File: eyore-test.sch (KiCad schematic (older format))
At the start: 29 parts, among them P1 USB_5PIN_SHELL, P2 CONN_01X04, P3 CONN_01X02, SW1 SW_PUSHBUTTON, SW2 SW_PUSHBUTTON, U1 LD1117S33CTR, U2 STM32F072C8, U3 ESP-12E, U4 ESP-12E

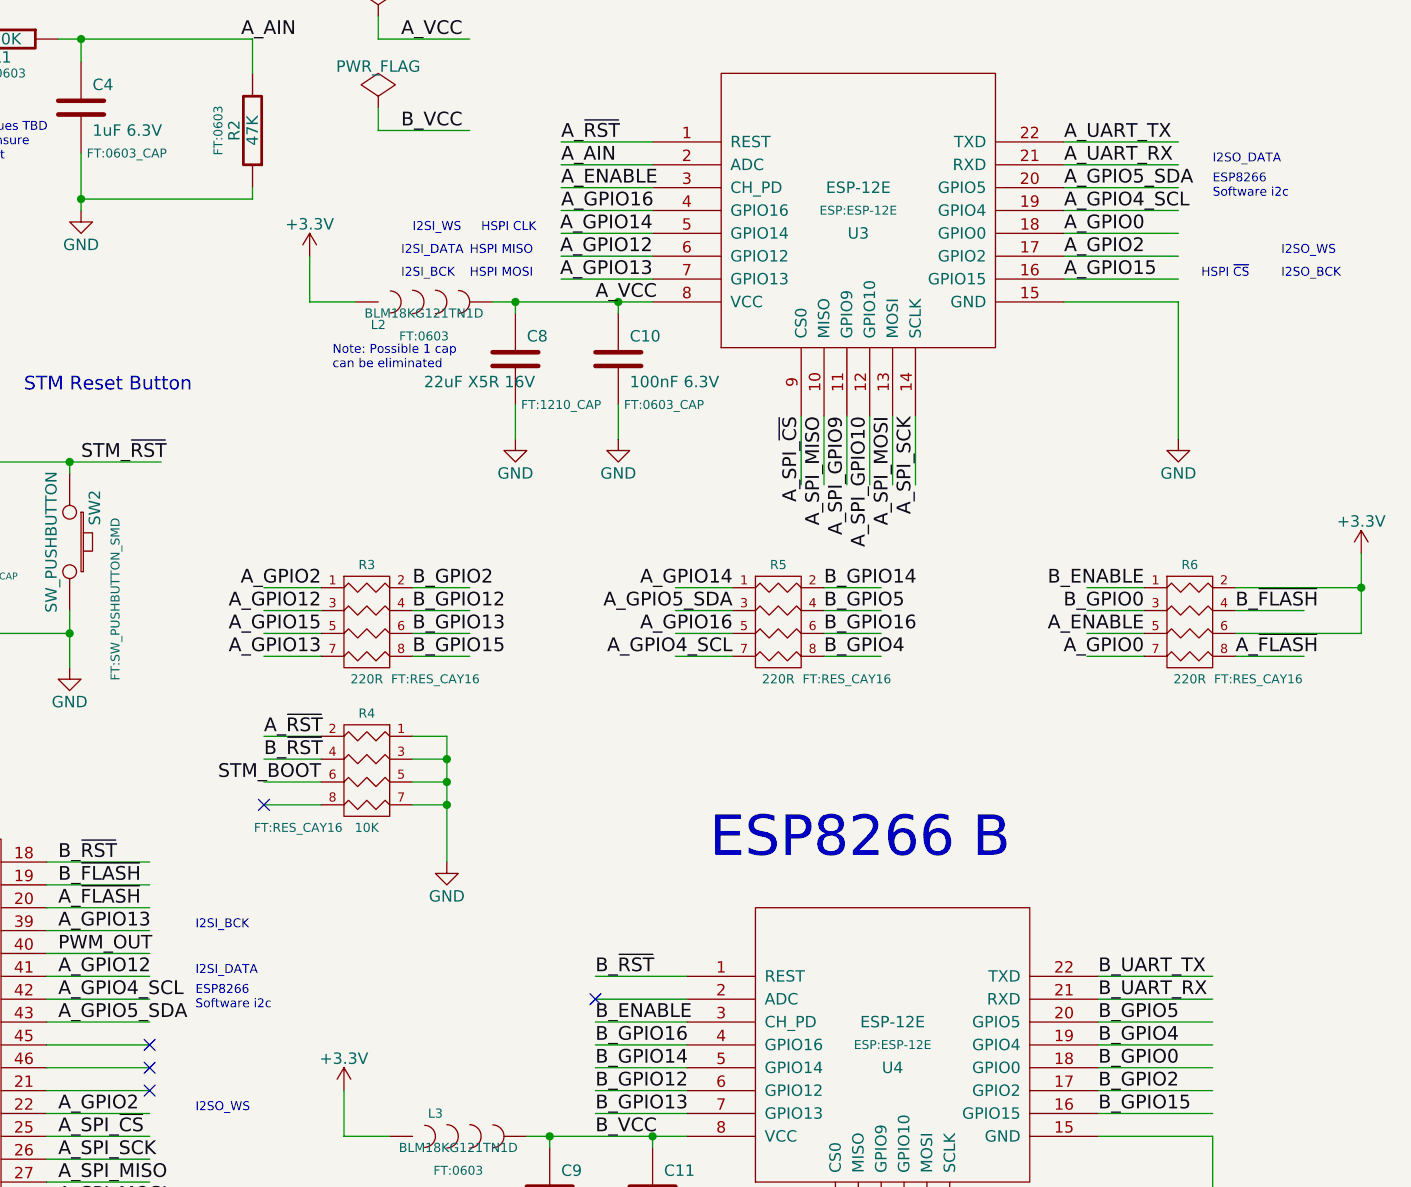
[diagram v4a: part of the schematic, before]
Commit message: Routed 4 layer version
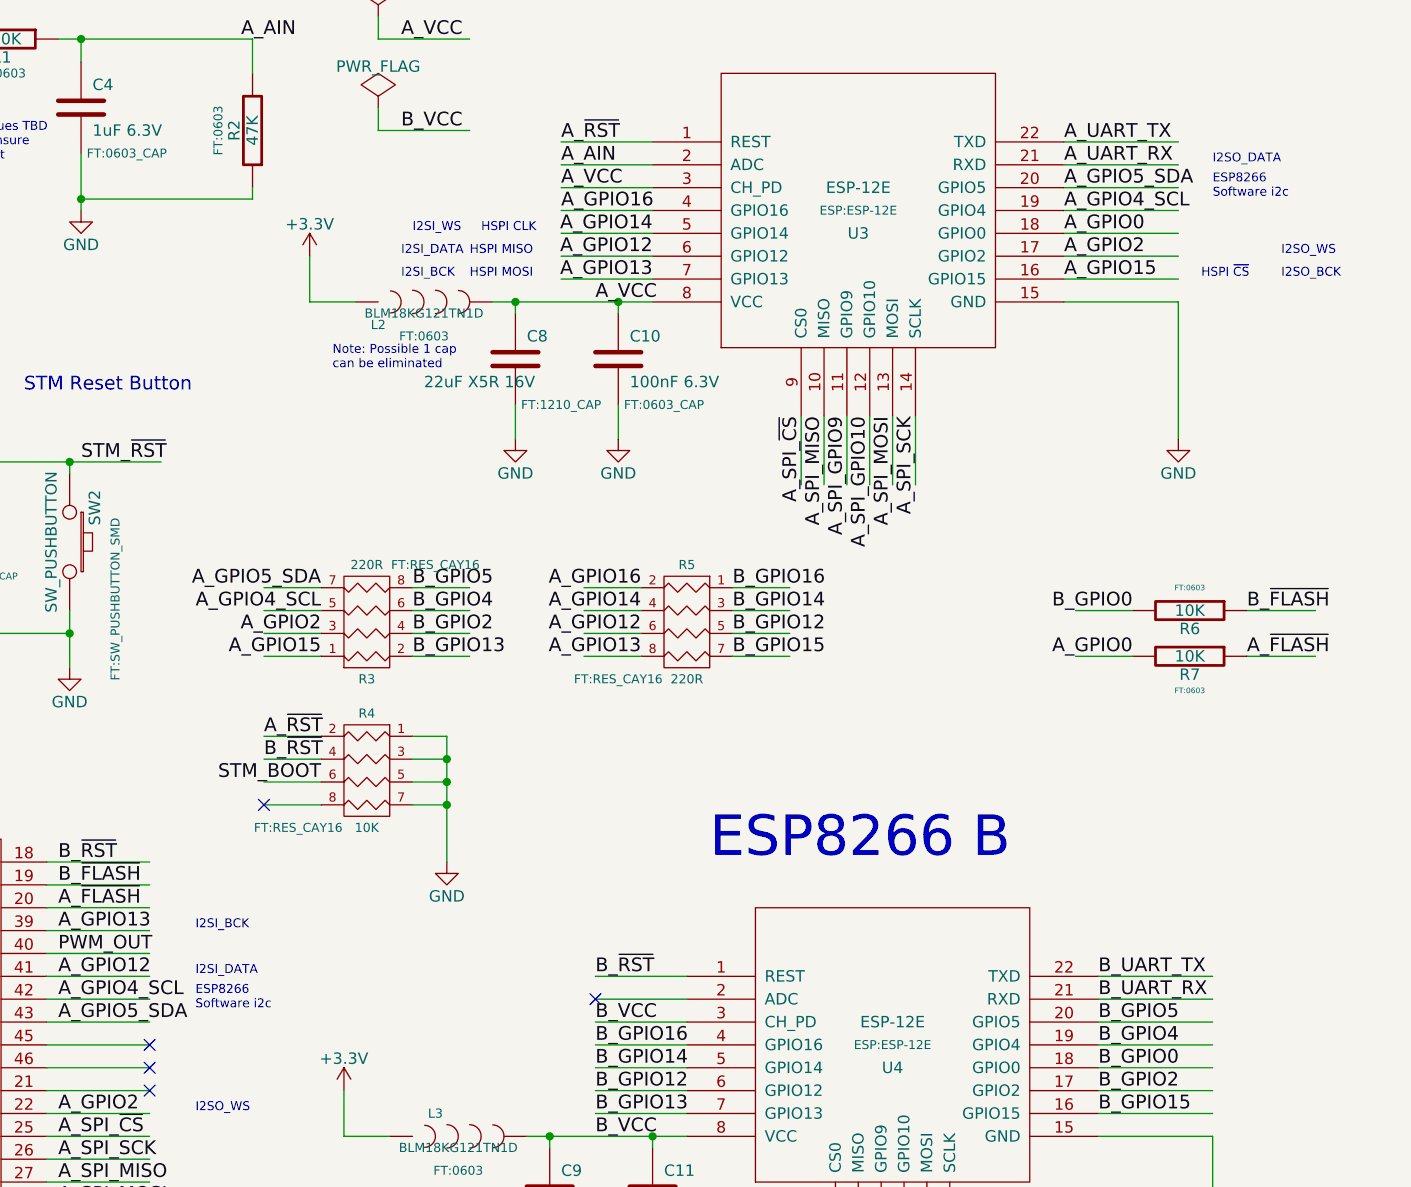
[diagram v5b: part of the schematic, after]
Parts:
- removed R6: 220R, FT:RES_CAY16, symbol R_PACK4
- added R6, R7: 10K, FT:0603, symbol R
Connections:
- net labels removed: A_ENABLE, B_ENABLE
- wire segments 189 -> 184
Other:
- moved on the sheet: R5
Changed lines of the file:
@@
 Text Label 7450 1350 0    60   ~ 0
 A_~RST
-Text Label 7450 1550 0    60   ~ 0
-A_ENABLE
 Text Label 9650 1750 0    60   ~ 0
 A_GPIO0
@@
 Text Label 7600 5000 0    60   ~ 0
 B_~RST
-Text Label 7600 5200 0    60   ~ 0
-B_ENABLE
 Text Label 9800 5400 0    60   ~ 0
 B_GPIO0
@@
 L R_PACK4 R3
 U 1 1 56319BA9
-P 6600 3650
-F 0 "R3" H 6600 4100 40  0000 C CNN
-F 1 "220R" H 6600 3600 40  0000 C CNN
-F 2 "FT:RES_CAY16" H 6900 3600 39  0000 C CNN
-F 3 "" H 6600 3650 60  0000 C CNN
-	1    6600 3650
-	1    0    0    -1
+P 6600 3250
+F 0 "R3" H 6600 3700 40  0000 C CNN
+F 1 "220R" H 6600 3200 40  0000 C CNN
+F 2 "FT:RES_CAY16" H 6900 3200 39  0000 C CNN
+F 3 "" H 6600 3250 60  0000 C CNN
+	1    6600 3250
+	1    0    0    1
 $EndComp
 Text Label 1550 4600 2    60   ~ 0
@@
 A_AIN
 NoConn ~ 7600 5100
-Text Label 8200 3500 2    60   ~ 0
+Text Label 7800 3300 2    60   ~ 0
 A_GPIO16
-Text Label 8200 3300 2    60   ~ 0
+Text Label 7800 3400 2    60   ~ 0
 A_GPIO14
-Text Label 10000 3600 2    60   ~ 0
+Text Label 9950 3600 2    60   ~ 0
 A_GPIO0
+Text Label 8200 3500 0    60   ~ 0
+B_GPIO12
+Text Label 8200 3400 0    60   ~ 0
+B_GPIO14
+Text Label 8200 3300 0    60   ~ 0
+B_GPIO16
+Text Label 6800 3600 0    60   ~ 0
+B_GPIO13
+Text Label 8200 3600 0    60   ~ 0
+B_GPIO15
 Text Label 6800 3400 0    60   ~ 0
-B_GPIO12
-Text Label 8600 3300 0    60   ~ 0
-B_GPIO14
-Text Label 8600 3500 0    60   ~ 0
-B_GPIO16
-Text Label 6800 3500 0    60   ~ 0
-B_GPIO13
-Text Label 6800 3600 0    60   ~ 0
-B_GPIO15
-Text Label 8600 3600 0    60   ~ 0
 B_GPIO4
-Text Label 8600 3400 0    60   ~ 0
+Text Label 6800 3300 0    60   ~ 0
 B_GPIO5
-Text Label 8200 3600 2    60   ~ 0
+Text Label 6400 3400 2    60   ~ 0
 A_GPIO4_SCL
-Text Label 8200 3400 2    60   ~ 0
+Text Label 6400 3300 2    60   ~ 0
 A_GPIO5_SDA
 Text Label 5250 5200 0    60   ~ 0
@@
 	-1   0    0    1
 $EndComp
-Text Label 6400 3600 2    60   ~ 0
+Text Label 7800 3600 2    60   ~ 0
 A_GPIO13
-Text Label 6400 3400 2    60   ~ 0
+Text Label 7800 3500 2    60   ~ 0
 A_GPIO12
 Text Label 1550 5000 2    60   ~ 0
@@
 Text Notes 5100 2450 0    60   ~ 0
 STM Reset Button
-Text Label 6400 3500 2    60   ~ 0
+Text Label 6400 3600 2    60   ~ 0
 A_GPIO15
 $Comp
-L +3.3V #PWR021
-U 1 1 5632C27E
-P 10950 3150
-F 0 "#PWR021" H 10950 3000 50  0001 C CNN
-F 1 "+3.3V" H 10950 3290 50  0000 C CNN
-F 2 "" H 10950 3150 60  0000 C CNN
-F 3 "" H 10950 3150 60  0000 C CNN
-	1    10950 3150
-	1    0    0    -1
-$EndComp
-$Comp
-L PWR_FLAG #FLG022
+L PWR_FLAG #FLG021
 U 1 1 5632C368
 P 6650 800
-F 0 "#FLG022" H 6650 895 50  0001 C CNN
+F 0 "#FLG021" H 6650 895 50  0001 C CNN
 F 1 "PWR_FLAG" H 6650 980 50  0000 C CNN
 F 2 "" H 6650 800 60  0000 C CNN
@@
 A_VCC
 $Comp
-L PWR_FLAG #FLG023
+L PWR_FLAG #FLG022
 U 1 1 5632C4E6
 P 6650 1200
-F 0 "#FLG023" H 6650 1295 50  0001 C CNN
+F 0 "#FLG022" H 6650 1295 50  0001 C CNN
 F 1 "PWR_FLAG" H 6650 1380 50  0000 C CNN
 F 2 "" H 6650 1200 60  0000 C CNN
@@
 B_VCC
 $Comp
-L PWR_FLAG #FLG024
+L PWR_FLAG #FLG023
 U 1 1 5632C7E0
 P 2700 4000
-F 0 "#FLG024" H 2700 4095 50  0001 C CNN
+F 0 "#FLG023" H 2700 4095 50  0001 C CNN
 F 1 "PWR_FLAG" H 2700 4180 50  0000 C CNN
 F 2 "" H 2700 4000 60  0000 C CNN
@@
 $EndComp
 $Comp
-L PWR_FLAG #FLG025
+L PWR_FLAG #FLG024
 U 1 1 5632CBA7
 P 2400 1700
-F 0 "#FLG025" H 2400 1795 50  0001 C CNN
+F 0 "#FLG024" H 2400 1795 50  0001 C CNN
 F 1 "PWR_FLAG" H 2400 1880 50  0000 C CNN
 F 2 "" H 2400 1700 60  0000 C CNN
@@
 	1    0    0    -1
 $EndComp
-Text Label 6800 3300 0    60   ~ 0
+Text Label 6800 3500 0    60   ~ 0
 B_GPIO2
-Text Label 6400 3300 2    60   ~ 0
+Text Label 6400 3500 2    60   ~ 0
 A_GPIO2
 $Comp
-L PWR_FLAG #FLG026
+L PWR_FLAG #FLG025
 U 1 1 5632D5E0
 P 2400 1300
-F 0 "#FLG026" H 2400 1395 50  0001 C CNN
+F 0 "#FLG025" H 2400 1395 50  0001 C CNN
 F 1 "PWR_FLAG" H 2400 1480 50  0000 C CNN
 F 2 "" H 2400 1300 60  0000 C CNN
@@
 L R_PACK4 R5
 U 1 1 563332AA
-P 8400 3650
-F 0 "R5" H 8400 4100 40  0000 C CNN
-F 1 "220R" H 8400 3600 40  0000 C CNN
-F 2 "FT:RES_CAY16" H 8700 3600 39  0000 C CNN
-F 3 "" H 8400 3650 60  0000 C CNN
-	1    8400 3650
-	1    0    0    -1
-$EndComp
-$Comp
-L R_PACK4 R6
-U 1 1 5633332C
-P 10200 3650
-F 0 "R6" H 10200 4100 40  0000 C CNN
-F 1 "220R" H 10200 3600 40  0000 C CNN
-F 2 "FT:RES_CAY16" H 10500 3600 39  0000 C CNN
-F 3 "" H 10200 3650 60  0000 C CNN
-	1    10200 3650
-	1    0    0    -1
-$EndComp
-Text Label 10000 3300 2    60   ~ 0
-B_ENABLE
-Text Label 10000 3500 2    60   ~ 0
-A_ENABLE
+P 8000 3650
+F 0 "R5" H 8000 4100 40  0000 C CNN
+F 1 "220R" H 8000 3600 40  0000 C CNN
+F 2 "FT:RES_CAY16" H 8300 3600 39  0000 C CNN
+F 3 "" H 8000 3650 60  0000 C CNN
+	1    8000 3650
+	-1   0    0    -1
+$EndComp
 Text Label 1550 5300 2    60   ~ 0
 B_GPIO15
@@
 	7600 5200 8000 5200
 Wire Wire Line
-	10000 3500 9750 3500
-Wire Wire Line
-	9750 3400 10000 3400
+	9700 3400 9950 3400
 Connection ~ 2400 1700
 Connection ~ 1950 1700
 Connection ~ 2400 1300
-Wire Wire Line
-	10000 3300 9750 3300
 Connection ~ 3250 4000
 Wire Wire Line
@@
 	5200 4500 5650 4500
 Wire Wire Line
-	8600 3600 8850 3600
-Wire Wire Line
-	8600 3500 8850 3500
-Wire Wire Line
-	8600 3400 8850 3400
-Wire Wire Line
-	8600 3300 8850 3300
-Wire Wire Line
-	8200 3600 7950 3600
-Wire Wire Line
-	8200 3500 7950 3500
-Wire Wire Line
-	8200 3400 7950 3400
-Wire Wire Line
-	8200 3300 7950 3300
+	8200 3600 8450 3600
+Wire Wire Line
+	8200 3500 8450 3500
+Wire Wire Line
+	8200 3400 8450 3400
+Wire Wire Line
+	8200 3300 8450 3300
+Wire Wire Line
+	7800 3600 7550 3600
+Wire Wire Line
+	7800 3500 7550 3500
+Wire Wire Line
+	7800 3400 7550 3400
+Wire Wire Line
+	7800 3300 7550 3300
 Wire Wire Line
 	6800 3600 7050 3600
@@
 Connection ~ 5700 6950
 $Comp
-L GND #PWR027
+L GND #PWR026
 U 1 1 56425794
 P 6250 7550
-F 0 "#PWR027" H 6250 7300 50  0001 C CNN
+F 0 "#PWR026" H 6250 7300 50  0001 C CNN
 F 1 "GND" H 6250 7400 50  0000 C CNN
 F 2 "" H 6250 7550 60  0000 C CNN
@@
 	6950 3950 6950 4500
 $Comp
-L GND #PWR028
+L GND #PWR027
 U 1 1 56438AB2
 P 6950 4500
-F 0 "#PWR028" H 6950 4250 50  0001 C CNN
+F 0 "#PWR027" H 6950 4250 50  0001 C CNN
 F 1 "GND" H 6950 4350 50  0000 C CNN
 F 2 "" H 6950 4500 60  0000 C CNN
@@
 Text Label 5250 4600 0    60   ~ 0
 B_~FLASH
-Text Label 10400 3600 0    60   ~ 0
+Text Label 10450 3600 0    60   ~ 0
 A_~FLASH
-Wire Wire Line
-	10950 3150 10950 3500
-Connection ~ 10950 3300
-Text Label 10400 3400 0    60   ~ 0
+Text Label 10450 3400 0    60   ~ 0
 B_~FLASH
 Wire Wire Line
-	10000 3600 9750 3600
-Wire Wire Line
-	10950 3500 10400 3500
-Text Label 10000 3400 2    60   ~ 0
+	9950 3600 9700 3600
+Text Label 9950 3400 2    60   ~ 0
 B_GPIO0
 Wire Wire Line
-	10400 3600 10700 3600
-Wire Wire Line
-	10400 3300 10950 3300
-Wire Wire Line
-	10400 3400 10700 3400
+	10450 3600 10750 3600
+Wire Wire Line
+	10450 3400 10750 3400
 Text Label 1350 2850 2    60   ~ 0
 STM_VCC
@@
 Text Label 4300 2700 2    60   ~ 0
 STM_VCC
+Text Label 7600 5200 0    60   ~ 0
+B_VCC
+Text Label 7450 1550 0    60   ~ 0
+A_VCC
+$Comp
+L R R7
+U 1 1 565D539D
+P 10200 3600
+F 0 "R7" V 10280 3600 50  0000 C CNN
+F 1 "10K" V 10200 3600 50  0000 C CNN
+F 2 "FT:0603" V 10350 3600 24  0000 C CNN
+F 3 "" H 10200 3600 60  0000 C CNN
+	1    10200 3600
+	0    1    1    0
+$EndComp
+$Comp
+L R R6
+U 1 1 565D5430
+P 10200 3400
+F 0 "R6" V 10280 3400 50  0000 C CNN
+F 1 "10K" V 10200 3400 50  0000 C CNN
+F 2 "FT:0603" V 10100 3400 24  0000 C CNN
+F 3 "" H 10200 3400 60  0000 C CNN
+	1    10200 3400
+	0    1    1    0
+$EndComp
 $EndSCHEMATC

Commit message: V1.0 as ordered
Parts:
- added TP1, TP2, TP3: TESTPOINT, FT:1X01, symbol TESTPOINT
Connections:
- wire segments 184 -> 186
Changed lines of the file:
@@
 $EndComp
 $Comp
-L +5V #PWR01
+L +5V #PWR103
 U 1 1 56305FEF
 P 1950 950
-F 0 "#PWR01" H 1950 800 50  0001 C CNN
+F 0 "#PWR103" H 1950 800 50  0001 C CNN
 F 1 "+5V" H 1950 1090 50  0000 C CNN
 F 2 "" H 1950 950 60  0000 C CNN
@@
 $EndComp
 $Comp
-L +3.3V #PWR02
+L +3.3V #PWR108
 U 1 1 5630644C
 P 3950 900
-F 0 "#PWR02" H 3950 750 50  0001 C CNN
+F 0 "#PWR108" H 3950 750 50  0001 C CNN
 F 1 "+3.3V" H 3950 1040 50  0000 C CNN
 F 2 "" H 3950 900 60  0000 C CNN
@@
 $EndComp
 $Comp
-L GND #PWR03
+L GND #PWR104
 U 1 1 56306479
 P 1950 2000
-F 0 "#PWR03" H 1950 1750 50  0001 C CNN
+F 0 "#PWR104" H 1950 1750 50  0001 C CNN
 F 1 "GND" H 1950 1850 50  0000 C CNN
 F 2 "" H 1950 2000 60  0000 C CNN
@@
 $EndComp
 $Comp
-L GND #PWR04
+L GND #PWR102
 U 1 1 56306497
 P 1150 2050
-F 0 "#PWR04" H 1150 1800 50  0001 C CNN
+F 0 "#PWR102" H 1150 1800 50  0001 C CNN
 F 1 "GND" H 1150 1900 50  0000 C CNN
 F 2 "" H 1150 2050 60  0000 C CNN
@@
 $EndComp
 $Comp
-L GND #PWR05
+L GND #PWR101
 U 1 1 56306BF9
 P 1100 3350
-F 0 "#PWR05" H 1100 3100 50  0001 C CNN
+F 0 "#PWR101" H 1100 3100 50  0001 C CNN
 F 1 "GND" H 1100 3200 50  0000 C CNN
 F 2 "" H 1100 3350 60  0000 C CNN
@@
 $EndComp
 $Comp
-L GND #PWR06
+L GND #PWR107
 U 1 1 56316BE1
 P 3300 2000
-F 0 "#PWR06" H 3300 1750 50  0001 C CNN
+F 0 "#PWR107" H 3300 1750 50  0001 C CNN
 F 1 "GND" H 3300 1850 50  0000 C CNN
 F 2 "" H 3300 2000 60  0000 C CNN
@@
 A_GPIO5_SDA
 $Comp
-L GND #PWR07
+L GND #PWR121
 U 1 1 5631751A
 P 10150 2650
-F 0 "#PWR07" H 10150 2400 50  0001 C CNN
+F 0 "#PWR121" H 10150 2400 50  0001 C CNN
 F 1 "GND" H 10150 2500 50  0000 C CNN
 F 2 "" H 10150 2650 60  0000 C CNN
@@
 $EndComp
 $Comp
-L +3.3V #PWR08
+L +3.3V #PWR114
 U 1 1 5631769D
 P 6350 1850
-F 0 "#PWR08" H 6350 1700 50  0001 C CNN
+F 0 "#PWR114" H 6350 1700 50  0001 C CNN
 F 1 "+3.3V" H 6350 1990 50  0000 C CNN
 F 2 "" H 6350 1850 60  0000 C CNN
@@
 A_GPIO12
 $Comp
-L GND #PWR09
+L GND #PWR119
 U 1 1 56317DB5
 P 7700 2650
-F 0 "#PWR09" H 7700 2400 50  0001 C CNN
+F 0 "#PWR119" H 7700 2400 50  0001 C CNN
 F 1 "GND" H 7700 2500 50  0000 C CNN
 F 2 "" H 7700 2650 60  0000 C CNN
@@
 $EndComp
 $Comp
-L GND #PWR010
+L GND #PWR117
 U 1 1 56318159
 P 7250 2650
-F 0 "#PWR010" H 7250 2400 50  0001 C CNN
+F 0 "#PWR117" H 7250 2400 50  0001 C CNN
 F 1 "GND" H 7250 2500 50  0000 C CNN
 F 2 "" H 7250 2650 60  0000 C CNN
@@
 B_GPIO5
 $Comp
-L GND #PWR011
+L GND #PWR122
 U 1 1 56319095
 P 10300 6300
-F 0 "#PWR011" H 10300 6050 50  0001 C CNN
+F 0 "#PWR122" H 10300 6050 50  0001 C CNN
 F 1 "GND" H 10300 6150 50  0000 C CNN
 F 2 "" H 10300 6300 60  0000 C CNN
@@
 $EndComp
 $Comp
-L +3.3V #PWR012
+L +3.3V #PWR115
 U 1 1 5631909C
 P 6500 5500
-F 0 "#PWR012" H 6500 5350 50  0001 C CNN
+F 0 "#PWR115" H 6500 5350 50  0001 C CNN
 F 1 "+3.3V" H 6500 5640 50  0000 C CNN
 F 2 "" H 6500 5500 60  0000 C CNN
@@
 B_GPIO12
 $Comp
-L GND #PWR013
+L GND #PWR120
 U 1 1 563190B5
 P 7850 6300
-F 0 "#PWR013" H 7850 6050 50  0001 C CNN
+F 0 "#PWR120" H 7850 6050 50  0001 C CNN
 F 1 "GND" H 7850 6150 50  0000 C CNN
 F 2 "" H 7850 6300 60  0000 C CNN
@@
 $EndComp
 $Comp
-L GND #PWR014
+L GND #PWR118
 U 1 1 563190C4
 P 7400 6300
-F 0 "#PWR014" H 7400 6050 50  0001 C CNN
+F 0 "#PWR118" H 7400 6050 50  0001 C CNN
 F 1 "GND" H 7400 6150 50  0000 C CNN
 F 2 "" H 7400 6300 60  0000 C CNN
@@
 PWM to RC ADC test circuit
 $Comp
-L GND #PWR015
+L GND #PWR110
 U 1 1 5631DA5C
 P 5350 1650
-F 0 "#PWR015" H 5350 1400 50  0001 C CNN
+F 0 "#PWR110" H 5350 1400 50  0001 C CNN
 F 1 "GND" H 5350 1500 50  0000 C CNN
 F 2 "" H 5350 1650 60  0000 C CNN
@@
 A_AIN
 $Comp
-L +3.3V #PWR016
+L +3.3V #PWR105
 U 1 1 563276CF
 P 2000 3850
-F 0 "#PWR016" H 2000 3700 50  0001 C CNN
+F 0 "#PWR105" H 2000 3700 50  0001 C CNN
 F 1 "+3.3V" H 2000 3990 50  0000 C CNN
 F 2 "" H 2000 3850 60  0000 C CNN
@@
 $EndComp
 $Comp
-L GND #PWR017
+L GND #PWR112
 U 1 1 563280A5
 P 5700 7550
-F 0 "#PWR017" H 5700 7300 50  0001 C CNN
+F 0 "#PWR112" H 5700 7300 50  0001 C CNN
 F 1 "GND" H 5700 7400 50  0000 C CNN
 F 2 "" H 5700 7550 60  0000 C CNN
@@
 $EndComp
 $Comp
-L GND #PWR018
+L GND #PWR111
 U 1 1 563280B2
 P 5350 7550
-F 0 "#PWR018" H 5350 7300 50  0001 C CNN
+F 0 "#PWR111" H 5350 7300 50  0001 C CNN
 F 1 "GND" H 5350 7400 50  0000 C CNN
 F 2 "" H 5350 7550 60  0000 C CNN
@@
 STM_VCC
 $Comp
-L GND #PWR019
+L GND #PWR106
 U 1 1 563282F2
 P 3000 7300
-F 0 "#PWR019" H 3000 7050 50  0001 C CNN
+F 0 "#PWR106" H 3000 7050 50  0001 C CNN
 F 1 "GND" H 3000 7150 50  0000 C CNN
 F 2 "" H 3000 7300 60  0000 C CNN
@@
 STM_~RST
 $Comp
-L GND #PWR020
+L GND #PWR109
 U 1 1 56329666
 P 5300 3650
-F 0 "#PWR020" H 5300 3400 50  0001 C CNN
+F 0 "#PWR109" H 5300 3400 50  0001 C CNN
 F 1 "GND" H 5300 3500 50  0000 C CNN
 F 2 "" H 5300 3650 60  0000 C CNN
@@
 A_GPIO15
 $Comp
-L PWR_FLAG #FLG021
+L PWR_FLAG #FLG104
 U 1 1 5632C368
 P 6650 800
-F 0 "#FLG021" H 6650 895 50  0001 C CNN
+F 0 "#FLG104" H 6650 895 50  0001 C CNN
 F 1 "PWR_FLAG" H 6650 980 50  0000 C CNN
 F 2 "" H 6650 800 60  0000 C CNN
@@
 A_VCC
 $Comp
-L PWR_FLAG #FLG022
+L PWR_FLAG #FLG105
 U 1 1 5632C4E6
 P 6650 1200
-F 0 "#FLG022" H 6650 1295 50  0001 C CNN
+F 0 "#FLG105" H 6650 1295 50  0001 C CNN
 F 1 "PWR_FLAG" H 6650 1380 50  0000 C CNN
 F 2 "" H 6650 1200 60  0000 C CNN
@@
 B_VCC
 $Comp
-L PWR_FLAG #FLG023
+L PWR_FLAG #FLG103
 U 1 1 5632C7E0
 P 2700 4000
-F 0 "#FLG023" H 2700 4095 50  0001 C CNN
+F 0 "#FLG103" H 2700 4095 50  0001 C CNN
 F 1 "PWR_FLAG" H 2700 4180 50  0000 C CNN
 F 2 "" H 2700 4000 60  0000 C CNN
@@
 $EndComp
 $Comp
-L PWR_FLAG #FLG024
+L PWR_FLAG #FLG102
 U 1 1 5632CBA7
 P 2400 1700
-F 0 "#FLG024" H 2400 1795 50  0001 C CNN
+F 0 "#FLG102" H 2400 1795 50  0001 C CNN
 F 1 "PWR_FLAG" H 2400 1880 50  0000 C CNN
 F 2 "" H 2400 1700 60  0000 C CNN
@@
 A_GPIO2
 $Comp
-L PWR_FLAG #FLG025
+L PWR_FLAG #FLG101
 U 1 1 5632D5E0
 P 2400 1300
-F 0 "#FLG025" H 2400 1395 50  0001 C CNN
+F 0 "#FLG101" H 2400 1395 50  0001 C CNN
 F 1 "PWR_FLAG" H 2400 1480 50  0000 C CNN
 F 2 "" H 2400 1300 60  0000 C CNN
@@
 	9650 1950 10150 1950
 Wire Wire Line
-	9650 1850 10150 1850
+	9650 1850 10550 1850
 Wire Wire Line
 	9650 1750 10150 1750
@@
 	7850 1650 7450 1650
 Wire Wire Line
-	7850 1450 7450 1450
+	7300 1450 7850 1450
 Wire Wire Line
 	7850 1350 7450 1350
@@
 Connection ~ 5700 6950
 $Comp
-L GND #PWR026
+L GND #PWR113
 U 1 1 56425794
 P 6250 7550
-F 0 "#PWR026" H 6250 7300 50  0001 C CNN
+F 0 "#PWR113" H 6250 7300 50  0001 C CNN
 F 1 "GND" H 6250 7400 50  0000 C CNN
 F 2 "" H 6250 7550 60  0000 C CNN
@@
 	6950 3950 6950 4500
 $Comp
-L GND #PWR027
+L GND #PWR116
 U 1 1 56438AB2
 P 6950 4500
-F 0 "#PWR027" H 6950 4250 50  0001 C CNN
+F 0 "#PWR116" H 6950 4250 50  0001 C CNN
 F 1 "GND" H 6950 4350 50  0000 C CNN
 F 2 "" H 6950 4500 60  0000 C CNN
@@
 	0    1    1    0
 $EndComp
+$Comp
+L TESTPOINT TP1
+U 1 1 5664B947
+P 7300 1450
+F 0 "TP1" H 7200 1450 40  0000 C CNN
+F 1 "TESTPOINT" H 7300 1700 30  0000 C CNN
+F 2 "FT:1X01" H 7300 1350 24  0000 C CNN
+F 3 "" H 7300 1450 60  0000 C CNN
+	1    7300 1450
+	1    0    0    -1
+$EndComp
+Connection ~ 7300 1450
+$Comp
+L TESTPOINT TP2
+U 1 1 5664BF8B
+P 10550 1850
+F 0 "TP2" H 10450 1900 40  0000 C CNN
+F 1 "TESTPOINT" H 10700 1950 30  0000 C CNN
+F 2 "FT:1X01" H 10550 1750 24  0000 C CNN
+F 3 "" H 10550 1850 60  0000 C CNN
+	1    10550 1850
+	1    0    0    -1
+$EndComp
+Connection ~ 10550 1850
+$Comp
+L TESTPOINT TP3
+U 1 1 5664CD86
+P 10550 2500
+F 0 "TP3" H 10650 2550 40  0000 C CNN
+F 1 "TESTPOINT" H 10550 2750 30  0000 C CNN
+F 2 "FT:1X01" H 10650 2500 24  0000 C CNN
+F 3 "" H 10550 2500 60  0000 C CNN
+	1    10550 2500
+	1    0    0    -1
+$EndComp
+Wire Wire Line
+	10550 2500 10550 2600
+Wire Wire Line
+	10550 2600 10150 2600
+Connection ~ 10150 2600
 $EndSCHEMATC
